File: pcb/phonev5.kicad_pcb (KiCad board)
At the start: 4 copper layers, 81 x 115.8 mm, 40 parts, among them J1 coin, J2 keypad, J3 display, J4 RJ9, J5 mic, J6 card_reader, J7 speaker, Q1 IRF9540N, U2 TDA2822M

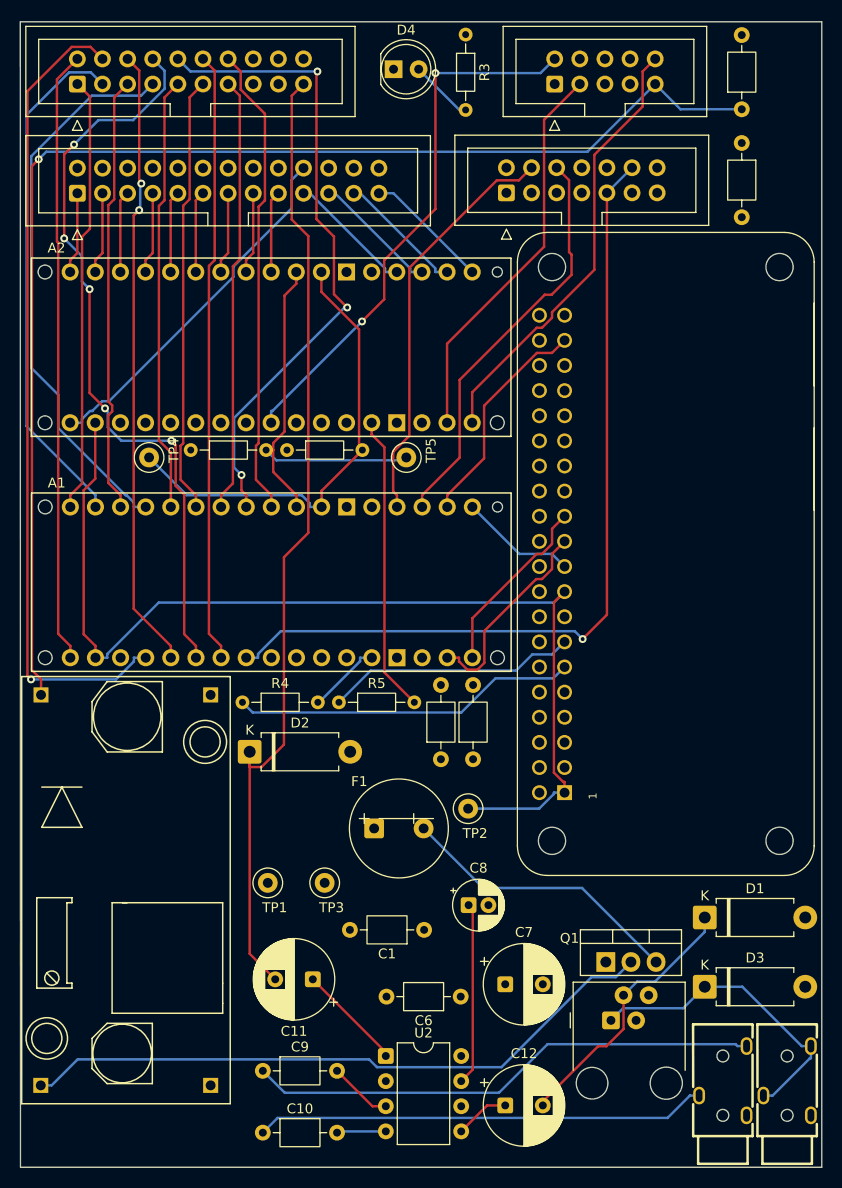
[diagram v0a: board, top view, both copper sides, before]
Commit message: pcb: Gerber export cleanup - RS-274X, export script for JLCPCB zip
- Disable Gerber X2 attributes (usegerberattributes no) to avoid JLCPCB
  preview parser issues
- Add export_jlcpcb.sh: Gerbers + drills -> phonev5-gerbers.zip
- BOM/CPL handled by KiCad JLCPCB plugin

Made-with: Cursor
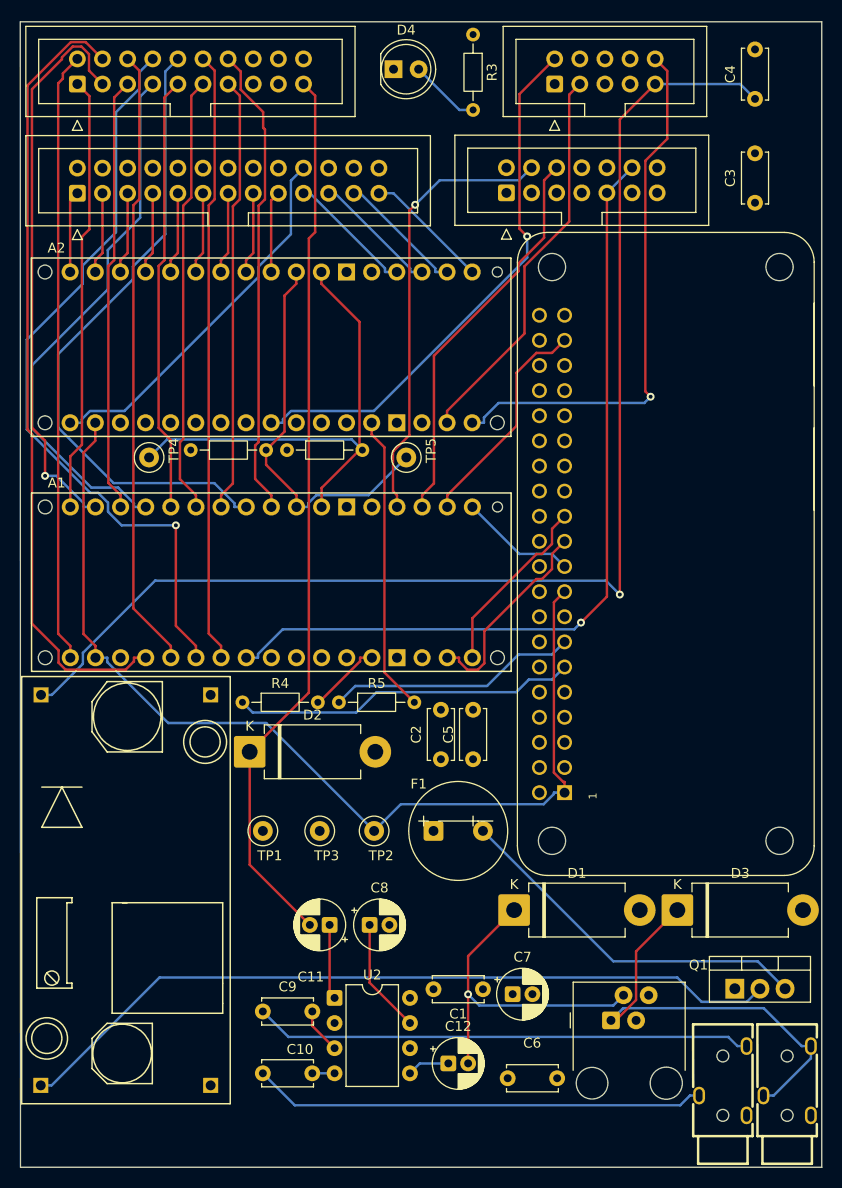
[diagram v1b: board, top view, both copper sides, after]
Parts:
- C1, C10, C2, C3, C4, C5, C6, C9: footprint Capacitor_THT:C_Axial_L3.8mm_D2.6mm_P7.50mm_Horizontal -> Capacitor_THT:C_Disc_D5.0mm_W2.5mm_P5.00mm
- C11, C12, C7: footprint Capacitor_THT:CP_Radial_D8.0mm_P3.80mm -> Capacitor_THT:CP_Radial_D5.0mm_P2.00mm
- D1, D2, D3: footprint Diode_THT:D_DO-15_P10.16mm_Horizontal -> Diode_THT:D_DO-201AD_P12.70mm_Horizontal
- moved D1 19.3 mm to (86.7, 133.5)
- moved Q1 13.3 mm to (109.0, 141.4)
- moved C6 12.8 mm to (91.0, 150.5)
- moved C8 10.2 mm to (72.0, 135.0)
- moved TP2 9.76 mm to (72.5, 125.5)
- moved C1 8.45 mm to (83.5, 141.5)
- moved D3 8.23 mm to (103.2, 133.5)
- moved U2 7.83 mm to (68.5, 142.4)
- moved C12 7.15 mm to (80.0, 149.0)
- moved C3 6.19 mm to (111.0, 62.0), turned to 90 degrees
- moved F1 6.01 mm to (78.5, 125.5)
- moved C10 6.00 mm to (61.2, 150.0)
- moved C9 6.00 mm to (61.2, 143.8)
- moved C11 5.76 mm to (68.0, 135.0)
- moved TP1 5.27 mm to (61.2, 125.5)
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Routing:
- net BOOST_IN+: track 65.5 -> 78.8 mm
- net mic+: track 31.7 -> 44.1 mm
- net coin_reset: track 44.8 -> 55.2 mm, vias 0 -> 1
- net speaker_front+: track 99.0 -> 90.7 mm
- net Net-(Q1-S): track 29.1 -> 37.1 mm
- net Net-(U2-RIPPLE): track 18.4 -> 11.6 mm
- net speaker_receiver+: track 27.3 -> 34.0 mm, vias 0 -> 1
- net key_col_2: track 52.5 -> 57.8 mm, vias 0 -> 1
- net 3.3V: track 106.9 -> 102.7 mm
- net mag_rdt: track 41.6 -> 45.0 mm, vias 0 -> 1
- net Net-(U2-OUT_A): track 10.8 -> 7.59 mm
- net sda: track 46.9 -> 50.0 mm
- net Net-(U2-IN_B): track 4.98 -> 2.25 mm
- net key_col_5: track 82.3 -> 79.6 mm, vias 1 -> 0
- net Net-(U2-IN_A): track 6.41 -> 4.64 mm
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
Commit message: pcb: checkpoint before THT→SMD migration
- 100nF caps: C_Disc_D5.0mm_W2.5mm_P2.50mm, LCSC C600221
- Preserve current state before replacing THT with SMD

Made-with: Cursor
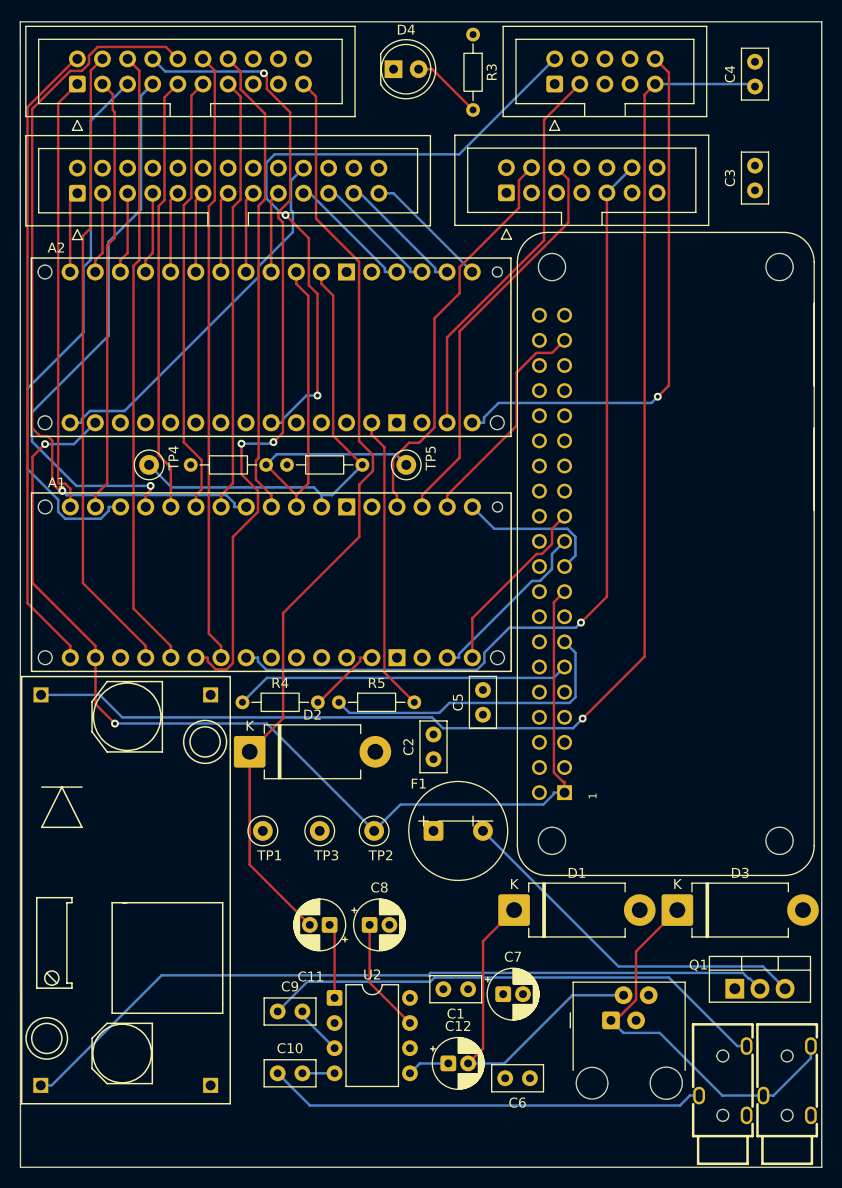
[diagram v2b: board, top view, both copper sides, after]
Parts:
- C1, C10, C2, C3, C4, C5, C6, C9: footprint Capacitor_THT:C_Disc_D5.0mm_W2.5mm_P5.00mm -> Capacitor_THT:C_Disc_D5.0mm_W2.5mm_P2.50mm
- moved C5 4.61 mm to (83.5, 113.8)
- moved C6 2.75 mm to (88.2, 150.5)
- moved C1 1.50 mm to (82.0, 141.5)
- moved C10 1.50 mm to (62.8, 150.0)
- moved C9 1.50 mm to (62.8, 143.8)
- moved R1 1.50 mm to (63.7, 88.5)
- moved R2 1.50 mm to (54.0, 88.5)
- moved C3 1.25 mm to (111.0, 60.8)
- moved C4 1.25 mm to (111.0, 50.2)
- moved C7 0.96 mm to (85.5, 142.0)
- moved C2 0.75 mm to (78.5, 118.2)
- moved TP4 0.75 mm to (49.8, 88.5)
- moved TP5 0.75 mm to (75.8, 88.5)
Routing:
- net key_col_5: track 79.6 -> 64.0 mm
- net key_col_2: track 57.8 -> 44.1 mm, vias 1 -> 0
- net key_hook_up: track 64.8 -> 78.2 mm, vias 0 -> 1
- net key_col_1: track 44.1 -> 56.0 mm
- net coin_tx: track 54.9 -> 65.4 mm, vias 1 -> 2
- net 3.3V: track 102.7 -> 111.1 mm, vias 0 -> 2
- net key_col_7: track 76.6 -> 83.5 mm, vias 1 -> 3
- net PI_RESET2: track 25.3 -> 31.1 mm
- net 12V_COIN: track 128.3 -> 133.9 mm
- net speaker_front+: track 90.7 -> 95.6 mm
- net scl: track 39.7 -> 44.1 mm
- net mag_rdt: track 45.0 -> 40.8 mm, vias 1 -> 0
- net mic+: track 44.1 -> 40.4 mm
- net sda: track 50.0 -> 46.5 mm
- net mosi: track 11.8 -> 15.1 mm
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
